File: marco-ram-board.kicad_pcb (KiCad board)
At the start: 4 copper layers, 160 x 100 mm, 185 parts, among them J201 PRG_USB, J202 MCU_RST, J203 MCU_BOOT0, J204 FT_TXD, J205 FT_RXD, J206 CONN_JTAG, J301 CONN_MCU_SERIAL, J302 CONN_EXT, J501 MCU_USB, J502 SD_Card, J503 CONN_DISP, J504 RJ45_Amphenol_RJMG1BD3B8K1ANR, J601 CONN_JACK_12V, J602 CONN_SCREW_12V, Q201 MMBT3906, Q601 DMP3037LSS, SW301 SW_RST, SW302 SW_BOOT0, SW501 BTN0, SW502 BTN1, SW503 BTN2, SW504 BTN3, SW601 PWR_SW, U201 FT2232HL, U301 STM32F765IITx, U401 IS42S86400D, U402 IS42S86400D, U403 IS42S86400D, U404 IS42S86400D, U405 IS42S86400D, U406 IS42S86400D, U407 IS42S86400D, U408 IS42S86400D, U501 KSZ8081RNA, U601 LM2576S-3.3, Y201 12MHz, Y301 25MHz

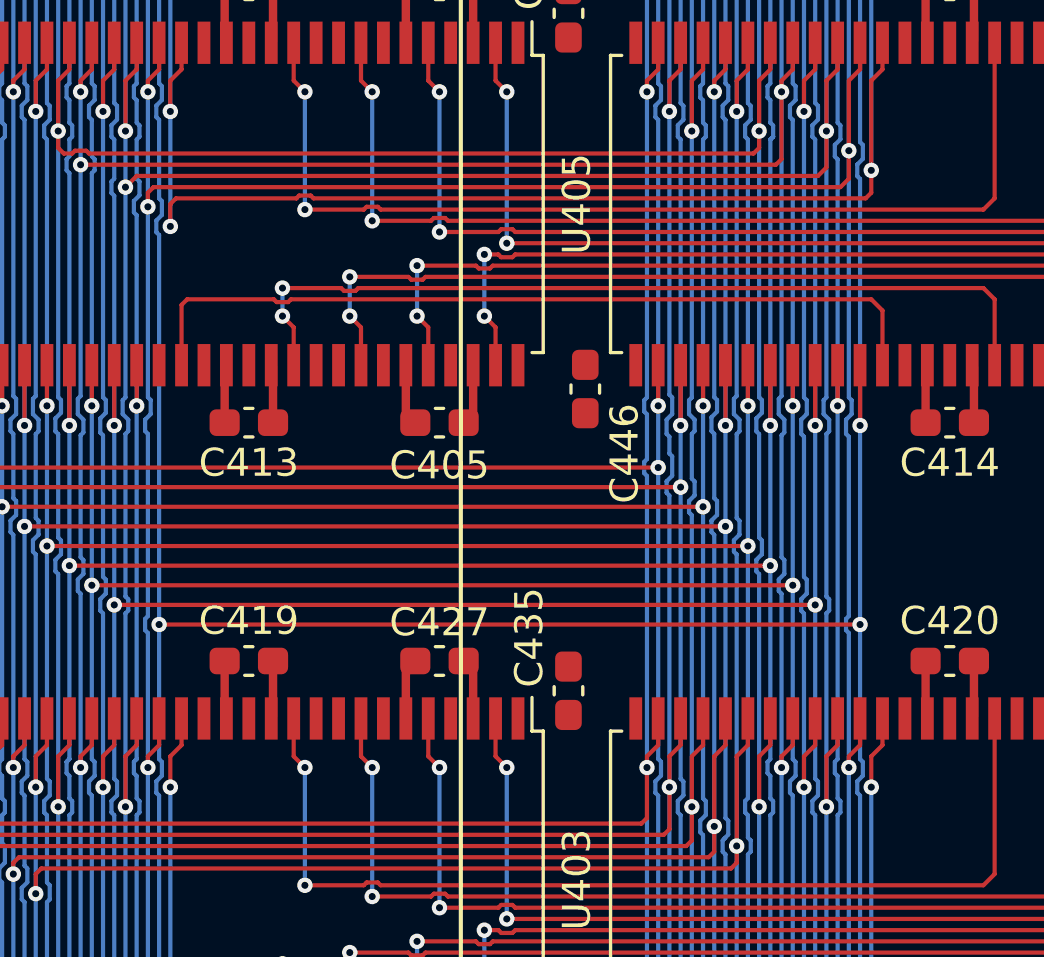
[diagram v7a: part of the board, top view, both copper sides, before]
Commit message: Fix missing connections in SDRAM.
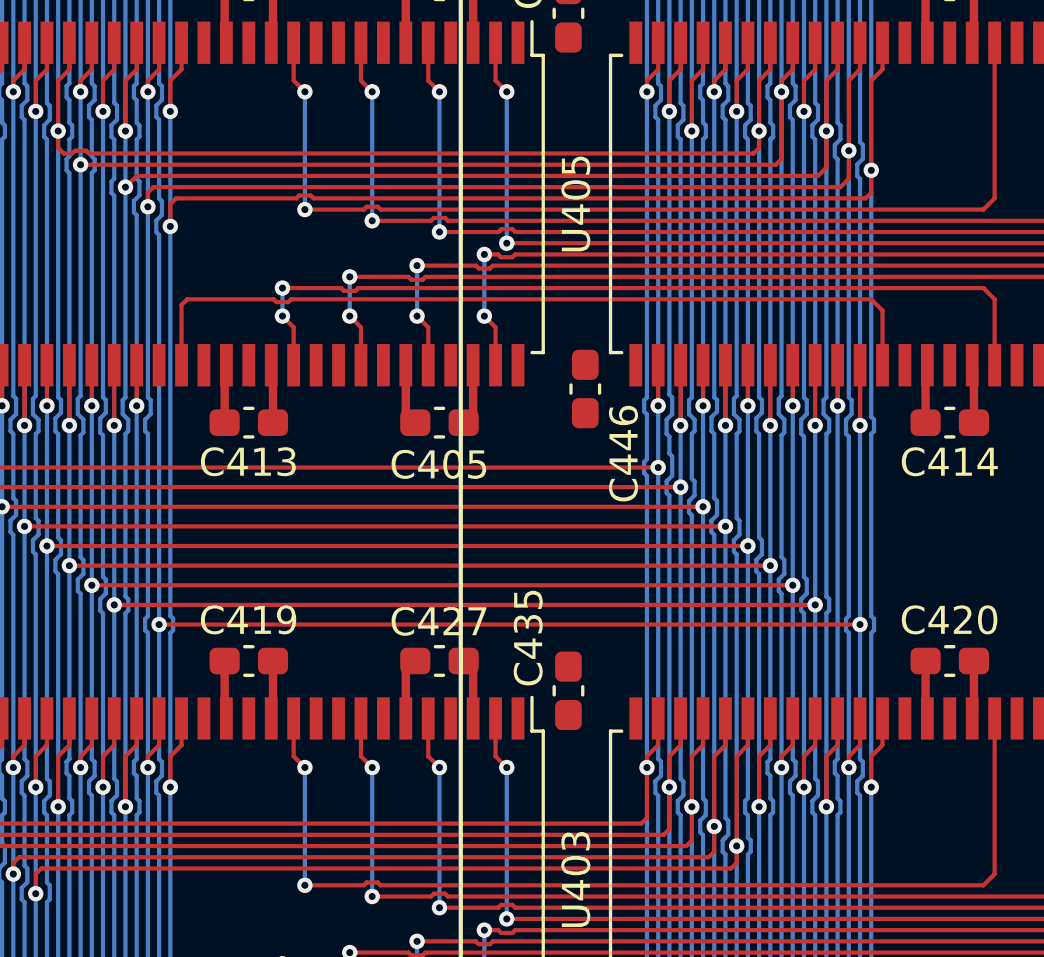
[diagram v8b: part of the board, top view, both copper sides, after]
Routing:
- net /mcu/SDRAM.~{WE}: track 136.4 -> 178.7 mm
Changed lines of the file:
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@@
   (segment (start 176.1 64.8) (end 176.1 65.2) (width 0.15) (layer "B.Cu") (net 167))
   (segment (start 201 65.3) (end 201.1 65.2) (width 0.15) (layer "B.Cu") (net 167))
+  (segment (start 201.1 93) (end 201 93.1) (width 0.15) (layer "B.Cu") (net 167))
   (segment (start 176 98.6) (end 176 108.8) (width 0.15) (layer "B.Cu") (net 167))
+  (segment (start 176.1 92.592893) (end 176.1 93) (width 0.15) (layer "B.Cu") (net 167))
+  (segment (start 176.1 93) (end 176 93.1) (width 0.15) (layer "B.Cu") (net 167))
   (segment (start 176.1 109.307107) (end 176 109.407107) (width 0.15) (layer "B.Cu") (net 167))
+  (segment (start 176 93.1) (end 176 98.6) (width 0.15) (layer "B.Cu") (net 167))
   (segment (start 201 98.6) (end 201 108.8) (width 0.15) (layer "B.Cu") (net 167))
   (segment (start 201 108.8) (end 201.1 108.9) (width 0.15) (layer "B.Cu") (net 167))
   (segment (start 201 64.7) (end 201 54.5) (width 0.15) (layer "B.Cu") (net 167))
   (segment (start 201.1 65.2) (end 201.1 64.8) (width 0.15) (layer "B.Cu") (net 167))
+  (segment (start 201 93.1) (end 201 98.6) (width 0.15) (layer "B.Cu") (net 167))
+  (segment (start 176 92.492893) (end 176.1 92.592893) (width 0.15) (layer "B.Cu") (net 167))
+  (segment (start 201.1 92.6) (end 201.1 93) (width 0.15) (layer "B.Cu") (net 167))
   (segment (start 201.1 108.9) (end 201.1 109.3) (width 0.15) (layer "B.Cu") (net 167))
+  (segment (start 201 92.5) (end 201.1 92.6) (width 0.15) (layer "B.Cu") (net 167))
+  (segment (start 201 86) (end 201 92.5) (width 0.15) (layer "B.Cu") (net 167))
   (segment (start 176 64.7) (end 176.1 64.8) (width 0.15) (layer "B.Cu") (net 167))
+  (segment (start 201.1 85.492893) (end 201.1 85.9) (width 0.15) (layer "B.Cu") (net 167))
+  (segment (start 176 78.6) (end 176 92.492893) (width 0.15) (layer "B.Cu") (net 167))
   (segment (start 176 74.5) (end 176 78.6) (width 0.15) (layer "B.Cu") (net 167))
   (segment (start 176.1 108.9) (end 176.1 109.307107) (width 0.15) (layer "B.Cu") (net 167))
   (segment (start 201.1 64.8) (end 201 64.7) (width 0.15) (layer "B.Cu") (net 167))
+  (segment (start 201 85.392893) (end 201.1 85.492893) (width 0.15) (layer "B.Cu") (net 167))
   (segment (start 176.1 65.2) (end 176 65.3) (width 0.15) (layer "B.Cu") (net 167))
   (segment (start 176 108.8) (end 176.1 108.9) (width 0.15) (layer "B.Cu") (net 167))
@@
   (segment (start 201 109.4) (end 201 118.6) (width 0.15) (layer "B.Cu") (net 167))
   (segment (start 201.1 109.3) (end 201 109.4) (width 0.15) (layer "B.Cu") (net 167))
+  (segment (start 201 76.6) (end 201 85.392893) (width 0.15) (layer "B.Cu") (net 167))
+  (segment (start 201.1 85.9) (end 201 86) (width 0.15) (layer "B.Cu") (net 167))
   (segment (start 201 65.3) (end 201 76.6) (width 0.15) (layer "B.Cu") (net 167))
   (segment (start 176 109.407107) (end 176 118.6) (width 0.15) (layer "B.Cu") (net 167))
